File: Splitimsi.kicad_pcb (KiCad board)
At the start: 2 copper layers, 118.2 x 99.3 mm, 30 parts, among them SW1 MX_RGB, SW10 MX_RGB, SW11 MX_RGB, SW12 MX_RGB, SW13 MX_RGB, SW14 MX_RGB, SW15 MX_RGB, SW16 MX_RGB, SW17 MX_RGB, SW18 MX_RGB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

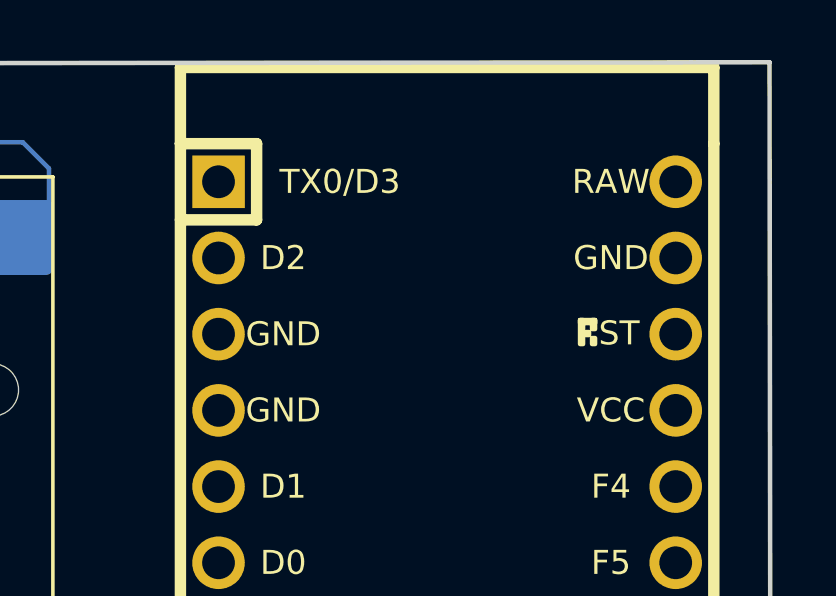
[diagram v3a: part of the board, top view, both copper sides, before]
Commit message: Reset button schematic added
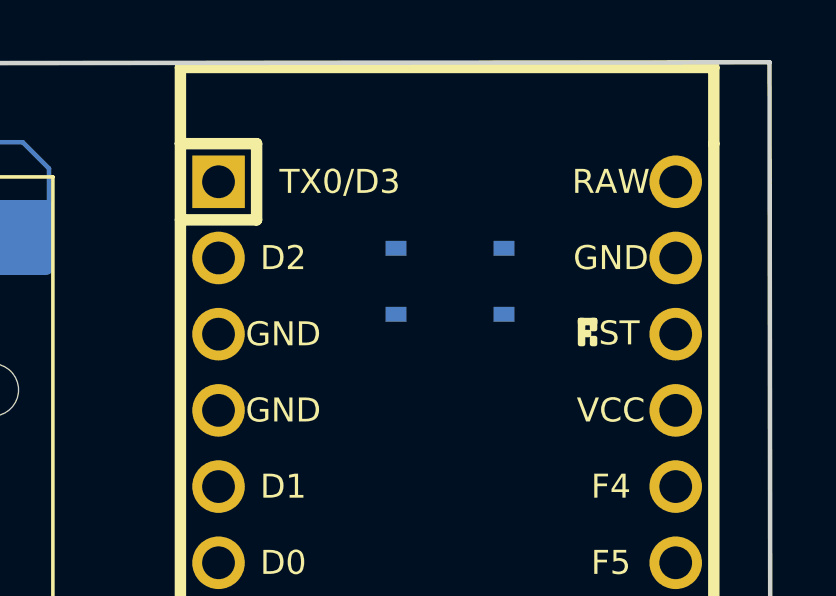
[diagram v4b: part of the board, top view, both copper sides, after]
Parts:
- added RST1: 1825910-6, Keebio-Parts:SW_SPST_3x3, B.Cu at (127.7, 25.0)
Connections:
- U1 pad 22: unconnected-(U1-Pad22) -> Net-(RST1-Pad1)
- U1 pad 23: GND -> Net-(RST1-Pad3)
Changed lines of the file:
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@@
   (net 85 "unconnected-(U1-Pad20)")
   (net 86 "/Row1")
-  (net 87 "unconnected-(U1-Pad22)")
+  (net 87 "Net-(RST1-Pad1)")
   (net 88 "/Row3")
   (net 89 "unconnected-(U1-Pad12)")
@@
   (net 95 "unconnected-(U2-Pad3)")
   (net 96 "/Row4_LedOut")
+  (net 97 "unconnected-(RST1-Pad2)")
+  (net 98 "Net-(RST1-Pad3)")
   (footprint "KeyboardCustomFPs:Kailh_HS_MX_LED" (layer "F.Cu")
     (at 107.95 85.725)
@@
       (net 3 "+5V") (pinfunction "VCC") (pintype "input"))
     (pad "22" thru_hole circle (at -8.89 -7.62 270) (size 1.7526 1.7526) (drill 1.0922) (layers *.Cu *.SilkS *.Mask)
-      (net 87 "unconnected-(U1-Pad22)") (pinfunction "RST") (pintype "input"))
+      (net 87 "Net-(RST1-Pad1)") (pinfunction "RST") (pintype "input"))
     (pad "23" thru_hole circle (at -11.43 -7.62 270) (size 1.7526 1.7526) (drill 1.0922) (layers *.Cu *.SilkS *.Mask)
-      (net 5 "GND") (pinfunction "GND") (pintype "input"))
+      (net 98 "Net-(RST1-Pad3)") (pinfunction "GND") (pintype "input"))
     (pad "24" thru_hole circle (at -13.97 -7.62 270) (size 1.7526 1.7526) (drill 1.0922) (layers *.Cu *.SilkS *.Mask)
       (net 90 "unconnected-(U1-Pad24)") (pinfunction "RAW") (pintype "input"))
@@
     )
   )
+  (footprint "Keebio-Parts:SW_SPST_3x3" (layer "B.Cu")
+    (at 127.652275 24.954886)
+    (descr "Low-profile SMD Tactile Switch, https://www.e-switch.com/system/asset/product_line/data_sheet/165/TL3342.pdf")
+    (tags "SPST Tactile Switch")
+    (property "Category" "Switches")
+    (property "DK_Datasheet_Link" "https://www.te.com/commerce/DocumentDelivery/DDEController?Action=srchrtrv&DocNm=1825910&DocType=Customer+Drawing&DocLang=English")
+    (property "DK_Detail_Page" "/product-detail/en/te-connectivity-alcoswitch-switches/1825910-6/450-1650-ND/1632536")
+    (property "Description" "SWITCH TACTILE SPST-NO 0.05A 24V")
+    (property "Digi-Key_PN" "450-1650-ND")
+    (property "Family" "Tactile Switches")
+    (property "MPN" "1825910-6")
+    (property "Manufacturer" "TE Connectivity ALCOSWITCH Switches")
+    (property "Sheetfile" "Splitimsi.kicad_sch")
+    (property "Sheetname" "")
+    (property "Status" "Active")
+    (attr smd)
+    (fp_text reference "RST1" (at 0 2.25) (layer "B.SilkS")
+      (effects (font (size 0.8 0.8) (thickness 0.15)) (justify mirror))
+    )
+    (fp_text value "1825910-6" (at 0 -2.5) (layer "B.Fab")
+      (effects (font (size 1 1) (thickness 0.15)) (justify mirror))
+    )
+    (fp_text user "${REFERENCE}" (at 0 2.25) (layer "B.Fab")
+      (effects (font (size 1 1) (thickness 0.15)) (justify mirror))
+    )
+    (fp_line (start -1.5 -1.5) (end 1.5 -1.5) (layer "B.SilkS") (width 0.12))
+    (fp_line (start -1.5 -1.5) (end -1.5 1.5) (layer "B.SilkS") (width 0.12))
+    (fp_line (start 1.5 -1.5) (end 1.5 1.5) (layer "B.SilkS") (width 0.12))
+    (fp_line (start -1.5 1.5) (end 1.5 1.5) (layer "B.SilkS") (width 0.12))
+    (fp_line (start -2.2 -1.6) (end 2.2 -1.6) (layer "B.CrtYd") (width 0.05))
+    (fp_line (start -2.2 1.6) (end -2.2 -1.6) (layer "B.CrtYd") (width 0.05))
+    (fp_line (start -2.2 1.6) (end 2.2 1.6) (layer "B.CrtYd") (width 0.05))
+    (fp_line (start 2.2 1.6) (end 2.2 -1.6) (layer "B.CrtYd") (width 0.05))
+    (fp_circle (center 0 0) (end 0.9 0) (layer "B.Fab") (width 0.1) (fill none))
+    (pad "1" smd rect locked (at 1.8 1.1) (size 0.7 0.5) (layers "B.Cu" "B.Paste" "B.Mask")
+      (net 87 "Net-(RST1-Pad1)") (pintype "passive"))
+    (pad "1" smd rect locked (at -1.8 1.1) (size 0.7 0.5) (layers "B.Cu" "B.Paste" "B.Mask")
+      (net 87 "Net-(RST1-Pad1)") (pintype "passive"))
+    (pad "2" smd rect locked (at -1.8 -1.1) (size 0.7 0.5) (layers "B.Cu" "B.Paste" "B.Mask")
+      (net 97 "unconnected-(RST1-Pad2)") (pintype "passive"))
+    (pad "2" smd rect locked (at 1.8 -1.1) (size 0.7 0.5) (layers "B.Cu" "B.Paste" "B.Mask")
+      (net 97 "unconnected-(RST1-Pad2)") (pintype "passive"))
+    (model "${KICAD6_3DMODEL_DIR}/Button_Switch_SMD.3dshapes/SW_SPST_PTS645.step"
+      (offset (xyz 0 0 0))
+      (scale (xyz 0.48 0.48 0.2))
+      (rotate (xyz 0 0 0))
+    )
+  )

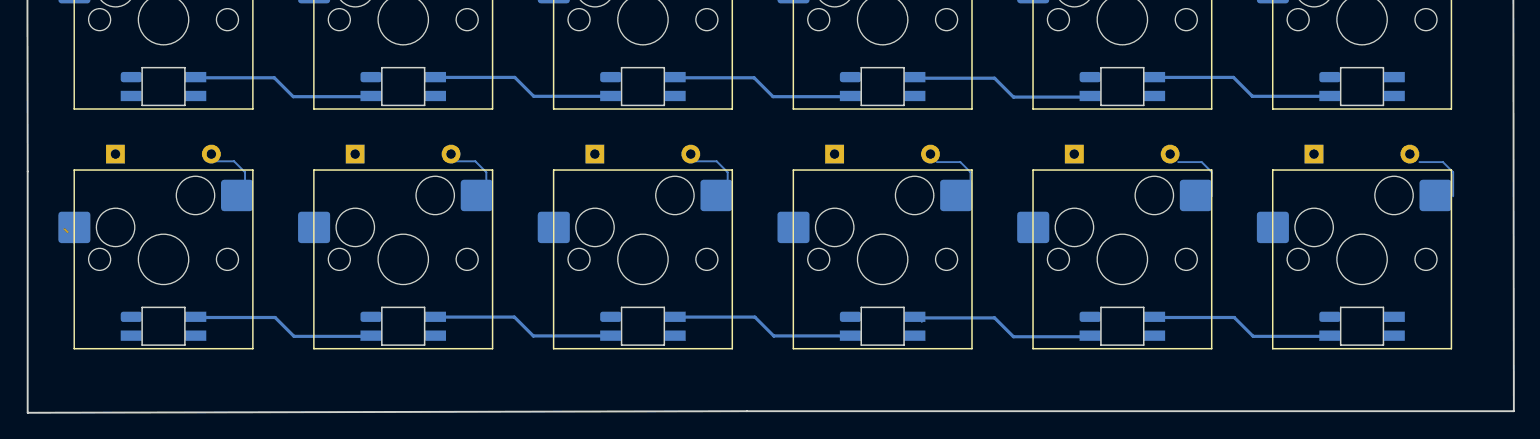
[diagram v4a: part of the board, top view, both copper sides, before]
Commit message: Led test route added between row 4 and 5
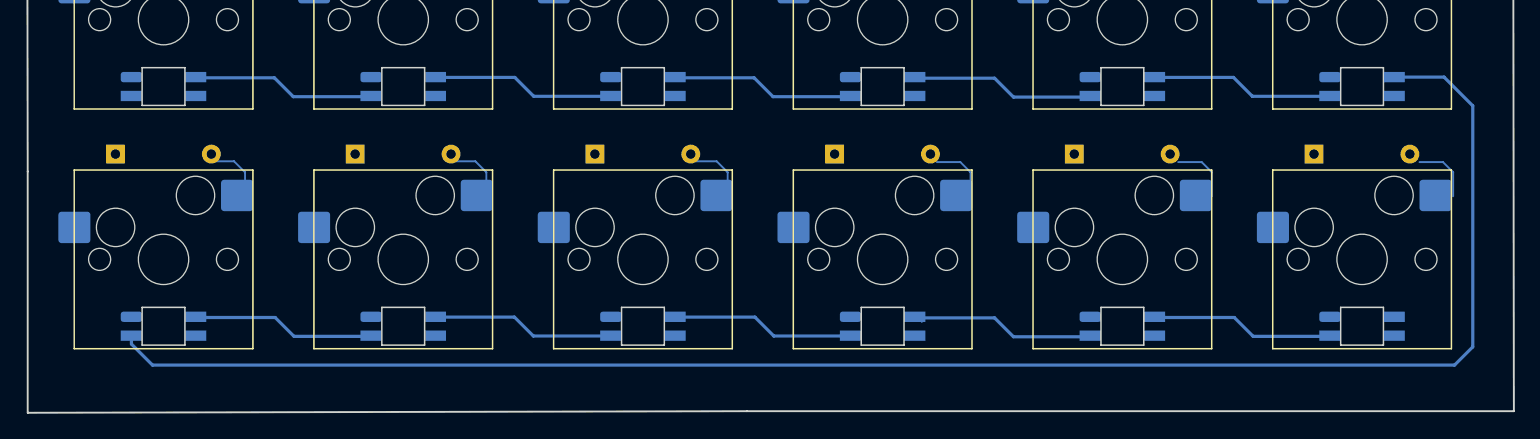
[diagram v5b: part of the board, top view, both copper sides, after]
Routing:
- net /Row3_LedOut: track 0.00 -> 134.9 mm
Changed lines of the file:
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@@
   (gr_line (start 20.32 97.79) (end 20.193 17.78) (layer "Edge.Cuts") (width 0.15))
   (gr_line (start 20.32 116.967) (end 20.32 97.79) (layer "Edge.Cuts") (width 0.15))
-  (segment (start 23.241 102.362) (end 23.495 102.616) (width 0.1524) (layer "F.Cu") (net 0))
   (segment (start 37.592 21.209) (end 37.592 23.114) (width 0.1524) (layer "B.Cu") (net 2))
   (segment (start 35.041761 20.335549) (end 36.718549 20.335549) (width 0.1524) (layer "B.Cu") (net 2))
@@
   (segment (start 36.718549 96.980049) (end 37.592 97.8535) (width 0.1524) (layer "B.Cu") (net 53))
   (segment (start 35.041761 96.980049) (end 36.718549 96.980049) (width 0.1524) (layer "B.Cu") (net 53))
+  (segment (start 28.563633 111.503178) (end 30.236171 113.175716) (width 0.254) (layer "B.Cu") (net 54))
+  (segment (start 28.563633 110.839178) (end 28.563633 111.503178) (width 0.254) (layer "B.Cu") (net 54))
+  (segment (start 133.716772 113.175716) (end 135.161707 111.730781) (width 0.254) (layer "B.Cu") (net 54))
+  (segment (start 132.88119 90.289178) (end 128.913633 90.289178) (width 0.254) (layer "B.Cu") (net 54))
+  (segment (start 135.161707 111.730781) (end 135.161707 92.569695) (width 0.254) (layer "B.Cu") (net 54))
+  (segment (start 135.161707 92.569695) (end 132.88119 90.289178) (width 0.254) (layer "B.Cu") (net 54))
+  (segment (start 30.236171 113.175716) (end 133.716772 113.175716) (width 0.254) (layer "B.Cu") (net 54))
   (segment (start 55.895549 96.980049) (end 56.769 97.8535) (width 0.1524) (layer "B.Cu") (net 55))
   (segment (start 56.769 97.8535) (end 56.769 99.7585) (width 0.1524) (layer "B.Cu") (net 55))

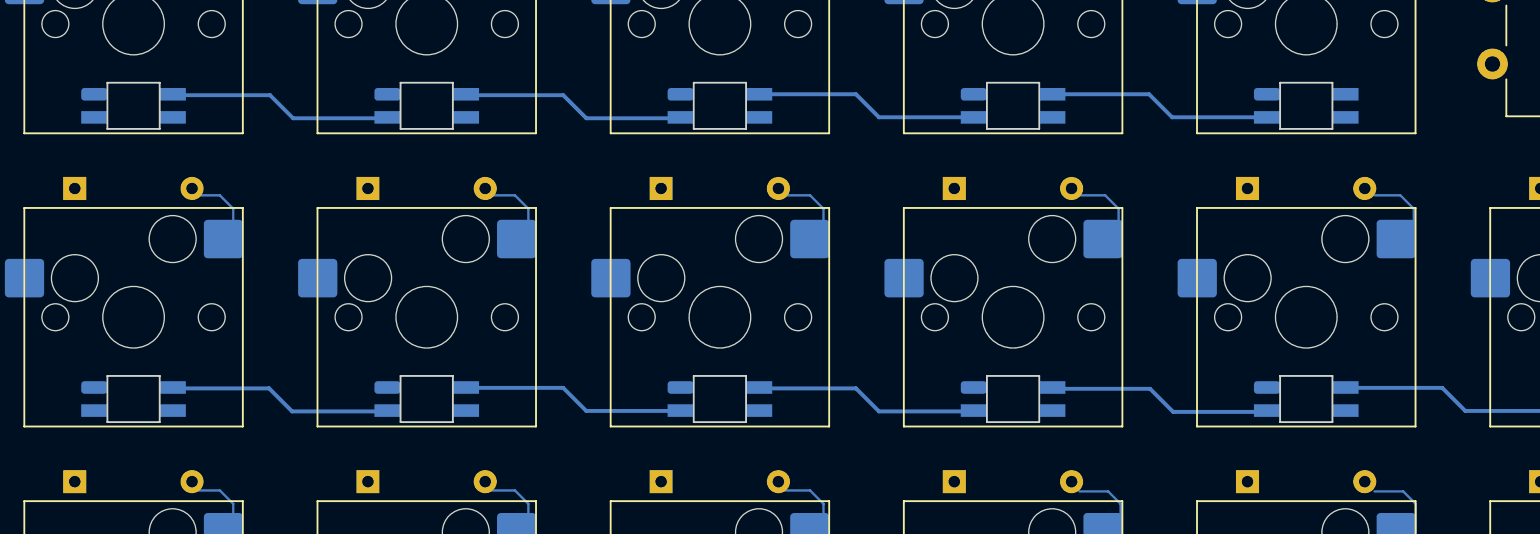
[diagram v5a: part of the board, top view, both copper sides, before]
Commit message: Led Connection added with via
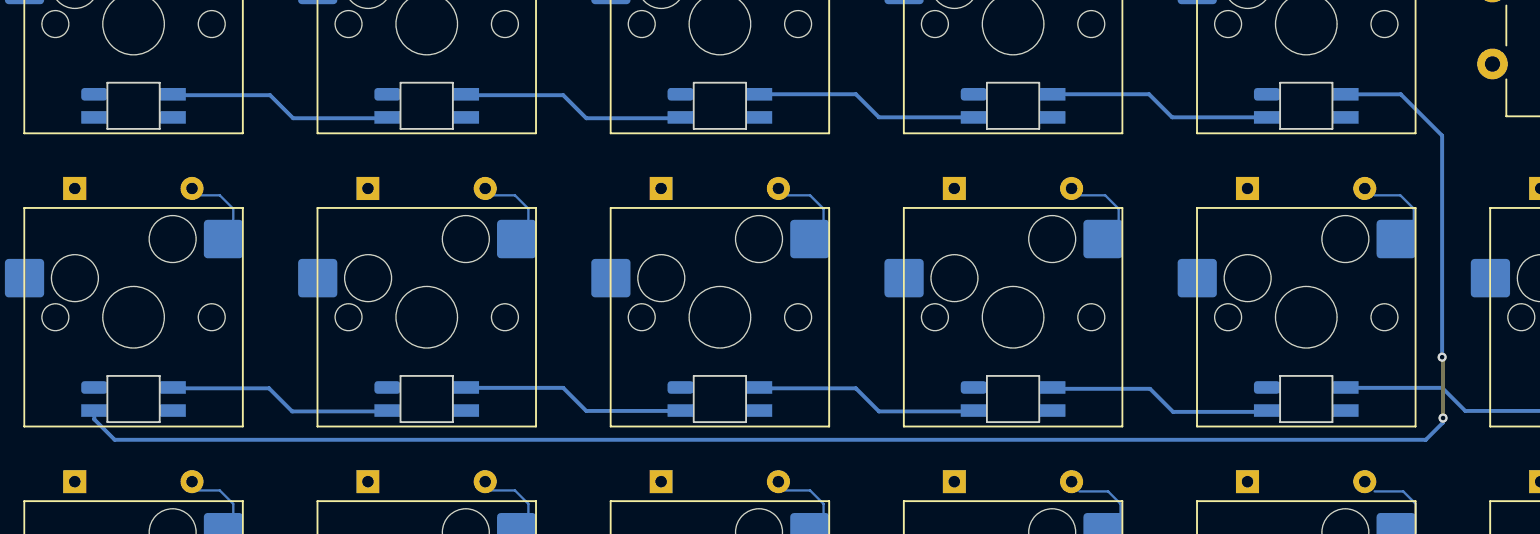
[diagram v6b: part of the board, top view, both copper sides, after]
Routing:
- net /Row2_LedOut: track 0.00 -> 115.3 mm, vias 0 -> 2
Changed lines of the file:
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@@
   (segment (start 75.072549 58.626049) (end 75.946 59.4995) (width 0.1524) (layer "B.Cu") (net 35))
   (segment (start 75.946 59.4995) (end 75.946 61.4045) (width 0.1524) (layer "B.Cu") (net 35))
+  (segment (start 116.200592 88.379686) (end 116.141597 88.320691) (width 0.254) (layer "F.Cu") (net 36))
+  (segment (start 116.200592 92.273362) (end 116.200592 88.379686) (width 0.254) (layer "F.Cu") (net 36))
+  (via (at 116.141597 88.320691) (size 0.6) (drill 0.3) (layers "F.Cu" "B.Cu") (net 36))
+  (via (at 116.200592 92.273362) (size 0.6) (drill 0.3) (layers "F.Cu" "B.Cu") (net 36))
+  (segment (start 116.141597 73.925889) (end 113.454886 71.239178) (width 0.254) (layer "B.Cu") (net 36))
+  (segment (start 28.563633 91.789178) (end 28.563633 92.362108) (width 0.254) (layer "B.Cu") (net 36))
+  (segment (start 116.141597 88.320691) (end 116.141597 73.925889) (width 0.254) (layer "B.Cu") (net 36))
+  (segment (start 115.079685 93.689244) (end 116.200592 92.568337) (width 0.254) (layer "B.Cu") (net 36))
+  (segment (start 116.200592 92.568337) (end 116.200592 92.273362) (width 0.254) (layer "B.Cu") (net 36))
+  (segment (start 28.563633 92.362108) (end 29.890769 93.689244) (width 0.254) (layer "B.Cu") (net 36))
+  (segment (start 113.454886 71.239178) (end 109.863633 71.239178) (width 0.254) (layer "B.Cu") (net 36))
+  (segment (start 29.890769 93.689244) (end 115.079685 93.689244) (width 0.254) (layer "B.Cu") (net 36))
   (segment (start 95.25 59.4995) (end 95.25 61.4045) (width 0.1524) (layer "B.Cu") (net 37))
   (segment (start 92.699761 58.626049) (end 94.376549 58.626049) (width 0.1524) (layer "B.Cu") (net 37))

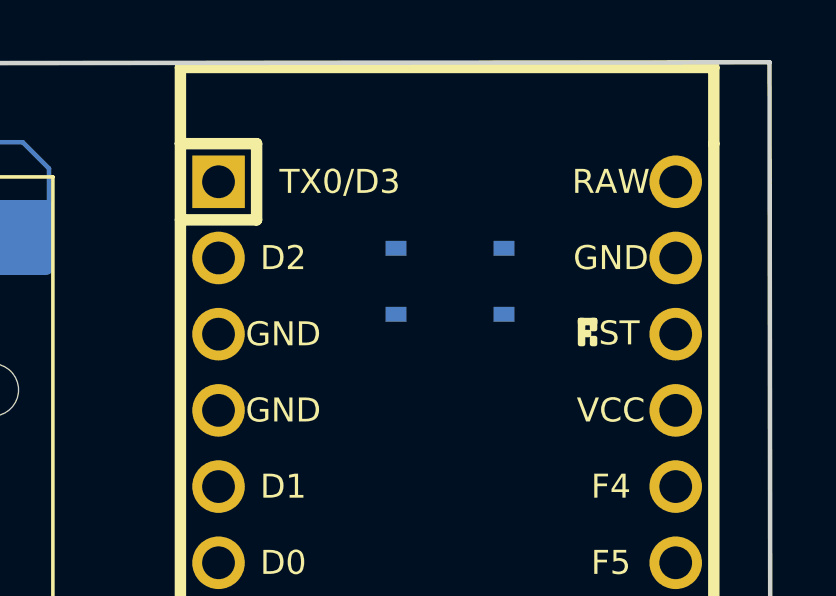
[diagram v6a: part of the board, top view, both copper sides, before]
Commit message: remove rst sw footprint
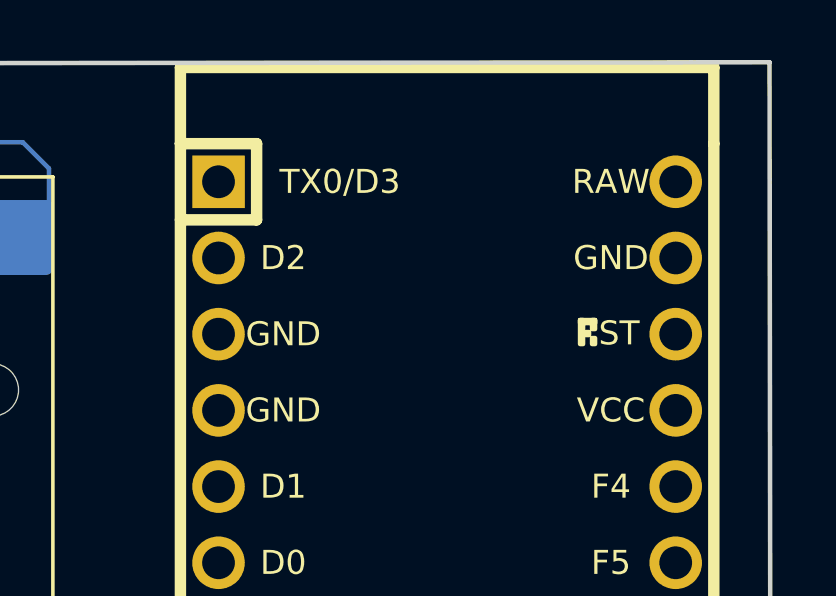
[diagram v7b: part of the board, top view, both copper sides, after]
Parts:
- removed RST1: 1825910-6, Keebio-Parts:SW_SPST_3x3
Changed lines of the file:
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@@
   (net 95 "unconnected-(U2-Pad3)")
   (net 96 "/Row4_LedOut")
-  (net 97 "unconnected-(RST1-Pad2)")
-  (net 98 "Net-(RST1-Pad3)")
+  (net 97 "Net-(RST1-Pad3)")
   (footprint "KeyboardCustomFPs:Kailh_HS_MX_LED" (layer "F.Cu")
     (at 107.95 85.725)
@@
       (net 87 "Net-(RST1-Pad1)") (pinfunction "RST") (pintype "input"))
     (pad "23" thru_hole circle (at -11.43 -7.62 270) (size 1.7526 1.7526) (drill 1.0922) (layers *.Cu *.SilkS *.Mask)
-      (net 98 "Net-(RST1-Pad3)") (pinfunction "GND") (pintype "input"))
+      (net 97 "Net-(RST1-Pad3)") (pinfunction "GND") (pintype "input"))
     (pad "24" thru_hole circle (at -13.97 -7.62 270) (size 1.7526 1.7526) (drill 1.0922) (layers *.Cu *.SilkS *.Mask)
       (net 90 "unconnected-(U1-Pad24)") (pinfunction "RAW") (pintype "input"))
@@
     )
   )
-  (footprint "Keebio-Parts:SW_SPST_3x3" (layer "B.Cu")
-    (at 127.652275 24.954886)
-    (descr "Low-profile SMD Tactile Switch, https://www.e-switch.com/system/asset/product_line/data_sheet/165/TL3342.pdf")
-    (tags "SPST Tactile Switch")
-    (property "Category" "Switches")
-    (property "DK_Datasheet_Link" "https://www.te.com/commerce/DocumentDelivery/DDEController?Action=srchrtrv&DocNm=1825910&DocType=Customer+Drawing&DocLang=English")
-    (property "DK_Detail_Page" "/product-detail/en/te-connectivity-alcoswitch-switches/1825910-6/450-1650-ND/1632536")
-    (property "Description" "SWITCH TACTILE SPST-NO 0.05A 24V")
-    (property "Digi-Key_PN" "450-1650-ND")
-    (property "Family" "Tactile Switches")
-    (property "MPN" "1825910-6")
-    (property "Manufacturer" "TE Connectivity ALCOSWITCH Switches")
-    (property "Sheetfile" "Splitimsi.kicad_sch")
-    (property "Sheetname" "")
-    (property "Status" "Active")
-    (attr smd)
-    (fp_text reference "RST1" (at 0 2.25) (layer "B.SilkS")
-      (effects (font (size 0.8 0.8) (thickness 0.15)) (justify mirror))
-    )
-    (fp_text value "1825910-6" (at 0 -2.5) (layer "B.Fab")
-      (effects (font (size 1 1) (thickness 0.15)) (justify mirror))
-    )
-    (fp_text user "${REFERENCE}" (at 0 2.25) (layer "B.Fab")
-      (effects (font (size 1 1) (thickness 0.15)) (justify mirror))
-    )
-    (fp_line (start -1.5 -1.5) (end 1.5 -1.5) (layer "B.SilkS") (width 0.12))
-    (fp_line (start -1.5 -1.5) (end -1.5 1.5) (layer "B.SilkS") (width 0.12))
-    (fp_line (start 1.5 -1.5) (end 1.5 1.5) (layer "B.SilkS") (width 0.12))
-    (fp_line (start -1.5 1.5) (end 1.5 1.5) (layer "B.SilkS") (width 0.12))
-    (fp_line (start -2.2 -1.6) (end 2.2 -1.6) (layer "B.CrtYd") (width 0.05))
-    (fp_line (start -2.2 1.6) (end -2.2 -1.6) (layer "B.CrtYd") (width 0.05))
-    (fp_line (start -2.2 1.6) (end 2.2 1.6) (layer "B.CrtYd") (width 0.05))
-    (fp_line (start 2.2 1.6) (end 2.2 -1.6) (layer "B.CrtYd") (width 0.05))
-    (fp_circle (center 0 0) (end 0.9 0) (layer "B.Fab") (width 0.1) (fill none))
-    (pad "1" smd rect locked (at 1.8 1.1) (size 0.7 0.5) (layers "B.Cu" "B.Paste" "B.Mask")
-      (net 87 "Net-(RST1-Pad1)") (pintype "passive"))
-    (pad "1" smd rect locked (at -1.8 1.1) (size 0.7 0.5) (layers "B.Cu" "B.Paste" "B.Mask")
-      (net 87 "Net-(RST1-Pad1)") (pintype "passive"))
-    (pad "2" smd rect locked (at -1.8 -1.1) (size 0.7 0.5) (layers "B.Cu" "B.Paste" "B.Mask")
-      (net 97 "unconnected-(RST1-Pad2)") (pintype "passive"))
-    (pad "2" smd rect locked (at 1.8 -1.1) (size 0.7 0.5) (layers "B.Cu" "B.Paste" "B.Mask")
-      (net 97 "unconnected-(RST1-Pad2)") (pintype "passive"))
-    (model "${KICAD6_3DMODEL_DIR}/Button_Switch_SMD.3dshapes/SW_SPST_PTS645.step"
-      (offset (xyz 0 0 0))
-      (scale (xyz 0.48 0.48 0.2))
-      (rotate (xyz 0 0 0))
-    )
-  )
